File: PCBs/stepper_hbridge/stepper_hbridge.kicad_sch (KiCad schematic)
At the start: 34 parts, among them J1 Conn_02x07_Odd_Even, J2 Conn_02x08_Odd_Even, J3 Conn_02x08_Odd_Even, J4 Conn_01x04_Pin, J5 Conn_01x04_Pin, J6 Conn_01x02_Pin, U1 L298N, U2 L298N, U3 NCP718xSN500

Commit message: fixed errors, need to add quadrature
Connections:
- net +24V: now also C1.1, C2.1, C3.1, C4.1, D11.1 (K), D14.1 (K), D16.1 (K), D5.1 (K), D6.1 (K), D7.1 (K), D8.1 (K), D9.1 (K), U1.4 (Vs), U2.4 (Vs); no longer C5.1, C6.1, U1.9 (Vss), U2.9 (Vss)
- net +5V: now also C5.1, C6.1, U1.9 (Vss), U2.9 (Vss); no longer C1.1, C2.1, C3.1, C4.1, D11.1 (K), D14.1 (K), D16.1 (K), D5.1 (K), D6.1 (K), D7.1 (K), D8.1 (K), D9.1 (K), U1.4 (Vs), U2.4 (Vs)
- net at D4.1 (K), D8.2 (A), U1.14 (OUT4): now also J4.3 (Pin_3); no longer J4.4 (Pin_4)
- net at D13.1 (K), D14.2 (A), U2.13 (OUT3): now also J5.4 (Pin_4); no longer J5.3 (Pin_3)
- net at D2.1 (K), D6.2 (A), U1.3 (OUT2): now also J4.1 (Pin_1); no longer J4.2 (Pin_2)
- net at D11.2 (A), D12.1 (K), U2.3 (OUT2): now also J5.1 (Pin_1); no longer J5.2 (Pin_2)
- net at D1.1 (K), D5.2 (A), U1.2 (OUT1): now also J4.2 (Pin_2); no longer J4.1 (Pin_1)
- net at D3.1 (K), D7.2 (A), U1.13 (OUT3): now also J4.4 (Pin_4); no longer J4.3 (Pin_3)
- net at D10.1 (K), D9.2 (A), U2.2 (OUT1): now also J5.2 (Pin_2); no longer J5.1 (Pin_1)
- net at D15.1 (K), D16.2 (A), U2.14 (OUT4): now also J5.3 (Pin_3); no longer J5.4 (Pin_4)
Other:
- moved on the sheet: D9

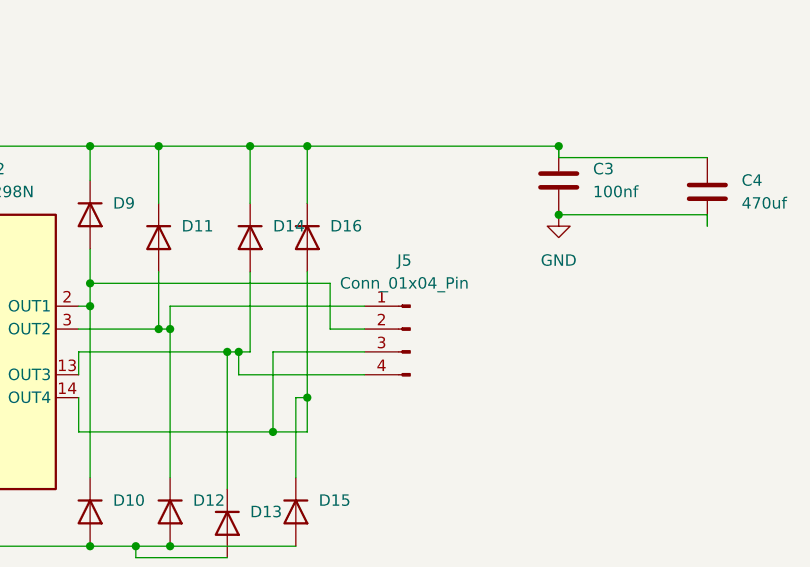
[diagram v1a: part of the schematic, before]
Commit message: stepper - changed diode placement, changed JSTXH to GH, changed main 24V connector
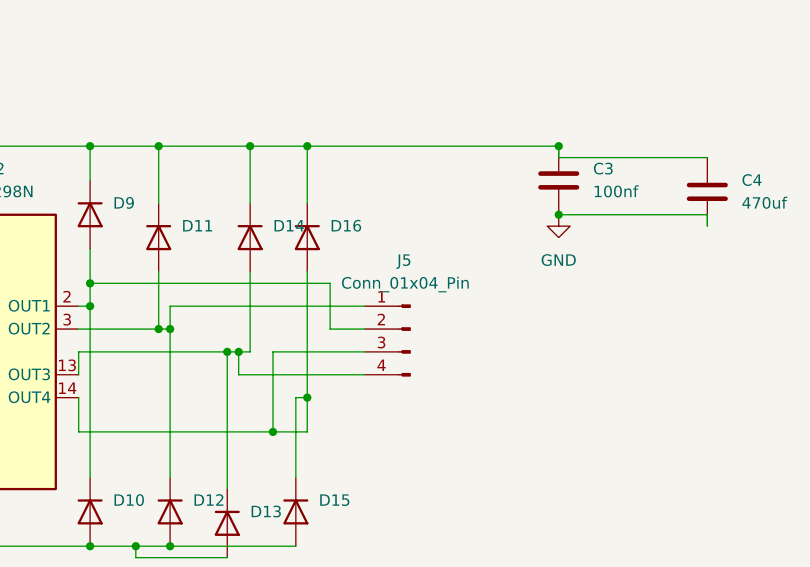
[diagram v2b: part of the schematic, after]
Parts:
- J4, J5: footprint Connector_JST:JST_XH_S4B-XH-SM4-TB_1x04-1MP_P2.50mm_Horizontal -> Connector_JST:JST_GH_SM04B-GHS-TB_1x04-1MP_P1.25mm_Horizontal
- J6: footprint Connector_JST:JST_XH_S2B-XH-A_1x02_P2.50mm_Horizontal -> Connector_Molex:Molex_Micro-Fit_3.0_43045-0212_2x01_P3.00mm_Vertical
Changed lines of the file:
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@@
 			)
 		)
-		(property "Footprint" "Connector_JST:JST_XH_S2B-XH-A_1x02_P2.50mm_Horizontal"
+		(property "Footprint" "Connector_Molex:Molex_Micro-Fit_3.0_43045-0212_2x01_P3.00mm_Vertical"
 			(at 384.81 55.88 0)
 			(effects
@@
 			)
 		)
-		(property "Footprint" "Connector_JST:JST_XH_S4B-XH-SM4-TB_1x04-1MP_P2.50mm_Horizontal"
+		(property "Footprint" "Connector_JST:JST_GH_SM04B-GHS-TB_1x04-1MP_P1.25mm_Horizontal"
 			(at 156.21 46.99 0)
 			(effects
@@
 		)
 		(property "Value" "Conn_01x04_Pin"
-			(at 318.135 71.12 0)
-			(effects
-				(font
-					(size 1.27 1.27)
-				)
-			)
-		)
-		(property "Footprint" "Connector_JST:JST_XH_S4B-XH-SM4-TB_1x04-1MP_P2.50mm_Horizontal"
+			(at 318.262 71.12 0)
+			(effects
+				(font
+					(size 1.27 1.27)
+				)
+			)
+		)
+		(property "Footprint" "Connector_JST:JST_GH_SM04B-GHS-TB_1x04-1MP_P1.25mm_Horizontal"
 			(at 318.77 76.2 0)
 			(effects

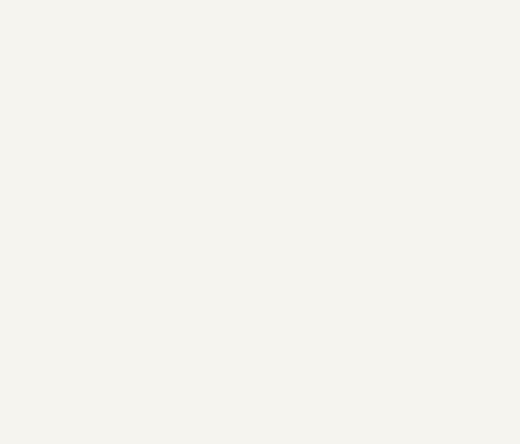
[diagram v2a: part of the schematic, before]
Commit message: both pcbs have smd capacitors, mounting holes, drc errors fixed
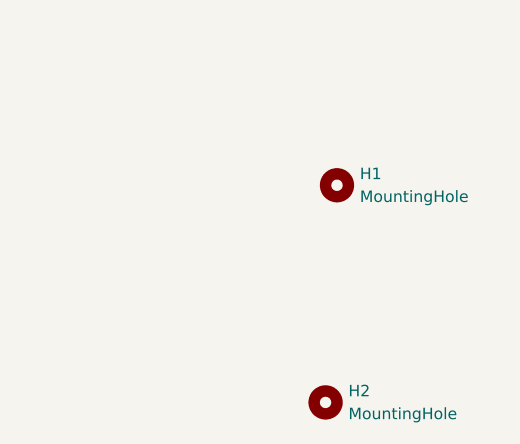
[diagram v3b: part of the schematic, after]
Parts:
- added H1, H2: MountingHole, MountingHole:MountingHole_3.2mm_M3, symbol Mechanical:MountingHole
- C2, C4: footprint Capacitor_THT:C_Radial_D8.0mm_H7.0mm_P3.50mm -> Capacitor_SMD:CP_Elec_6.3x7.7
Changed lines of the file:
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@@
 			)
 		)
-		(property "Footprint" "Capacitor_THT:C_Radial_D8.0mm_H7.0mm_P3.50mm"
+		(property "Footprint" "Capacitor_SMD:CP_Elec_6.3x7.7"
 			(at 352.7552 64.77 0)
 			(effects
@@
 			)
 		)
-		(property "Footprint" "Capacitor_THT:C_Radial_D8.0mm_H7.0mm_P3.50mm"
+		(property "Footprint" "Capacitor_SMD:CP_Elec_6.3x7.7"
 			(at 190.1952 35.56 0)
 			(effects
@@
 				(path "/705004fe-9694-4831-a243-8c72357320a8"
 					(reference "#PWR021")
+					(unit 1)
+				)
+			)
+		)
+	)
+	(symbol
+		(lib_id "Mechanical:MountingHole")
+		(at 535.94 128.27 0)
+		(unit 1)
+		(exclude_from_sim no)
+		(in_bom no)
+		(on_board yes)
+		(dnp no)
+		(fields_autoplaced yes)
+		(property "Reference" "H2"
+			(at 538.48 126.9999 0)
+			(effects
+				(font
+					(size 1.27 1.27)
+				)
+				(justify left)
+			)
+		)
+		(property "Value" "MountingHole"
+			(at 538.48 129.5399 0)
+			(effects
+				(font
+					(size 1.27 1.27)
+				)
+				(justify left)
+			)
+		)
+		(property "Footprint" "MountingHole:MountingHole_3.2mm_M3"
+			(at 535.94 128.27 0)
+			(effects
+				(font
+					(size 1.27 1.27)
+				)
+				(hide yes)
+			)
+		)
+		(property "Datasheet" "~"
+			(at 535.94 128.27 0)
+			(effects
+				(font
+					(size 1.27 1.27)
+				)
+				(hide yes)
+			)
+		)
+		(property "Description" "Mounting Hole without connection"
+			(at 535.94 128.27 0)
+			(effects
+				(font
+					(size 1.27 1.27)
+				)
+				(hide yes)
+			)
+		)
+		(instances
+			(project "stepper_hbridge"
+				(path "/705004fe-9694-4831-a243-8c72357320a8"
+					(reference "H2")
 					(unit 1)
 				)
@@
 					(unit 1)
 				)
+			)
+		)
+	)
+	(symbol
+		(lib_id "Mechanical:MountingHole")
+		(at 537.21 104.14 0)
+		(unit 1)
+		(exclude_from_sim no)
+		(in_bom no)
+		(on_board yes)
+		(dnp no)
+		(fields_autoplaced yes)
+		(property "Reference" "H1"
+			(at 539.75 102.8699 0)
+			(effects
+				(font
+					(size 1.27 1.27)
+				)
+				(justify left)
+			)
+		)
+		(property "Value" "MountingHole"
+			(at 539.75 105.4099 0)
+			(effects
+				(font
+					(size 1.27 1.27)
+				)
+				(justify left)
+			)
+		)
+		(property "Footprint" "MountingHole:MountingHole_3.2mm_M3"
+			(at 537.21 104.14 0)
+			(effects
+				(font
+					(size 1.27 1.27)
+				)
+				(hide yes)
+			)
+		)
+		(property "Datasheet" "~"
+			(at 537.21 104.14 0)
+			(effects
+				(font
+					(size 1.27 1.27)
+				)
+				(hide yes)
+			)
+		)
+		(property "Description" "Mounting Hole without connection"
+			(at 537.21 104.14 0)
+			(effects
+				(font
+					(size 1.27 1.27)
+				)
+				(hide yes)
+			)
+		)
+		(instances
+			(project ""
+				(path "/705004fe-9694-4831-a243-8c72357320a8"
+					(reference "H1")
+					(unit 1)
+				)

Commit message: fixed 3.3V, fized header
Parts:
- J6: footprint Connector_Molex:Molex_Micro-Fit_3.0_43045-0212_2x01_P3.00mm_Vertical -> footprints:CONN_SD-43045-001_02_MOL
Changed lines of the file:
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@@
 			)
 		)
-		(property "Footprint" "Connector_Molex:Molex_Micro-Fit_3.0_43045-0212_2x01_P3.00mm_Vertical"
+		(property "Footprint" "footprints:CONN_SD-43045-001_02_MOL"
 			(at 384.81 55.88 0)
 			(effects
